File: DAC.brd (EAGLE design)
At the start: 81.3 x 82.5 mm, 101 parts, among them IC1 LM2662, IC2 PCM1793, IC3 OPA2134PA, IC4 LMH6643, J1 USBSMD, J2 RCJ-21XXMILL, U1 LDO-TPS78233, U2 PCM2707, Y1 12MHz/20pF

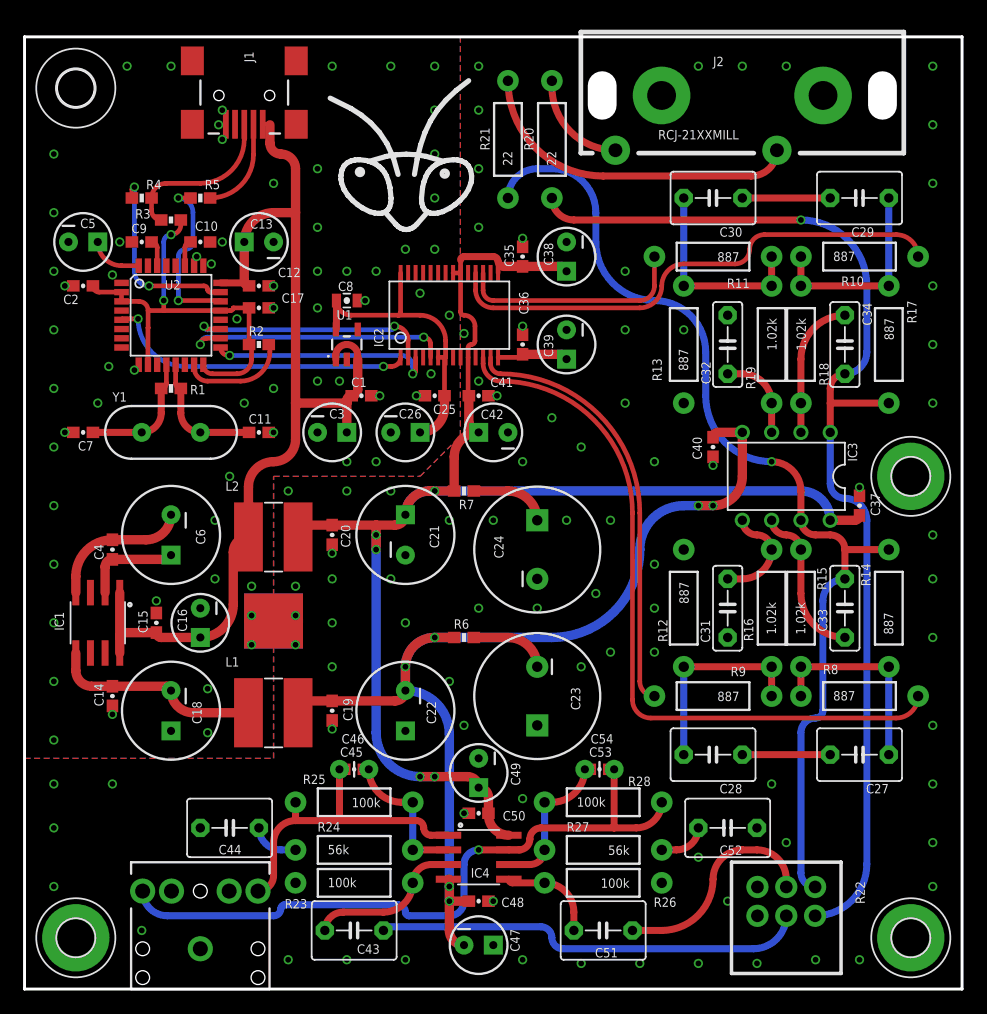
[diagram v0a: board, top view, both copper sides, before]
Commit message: PCB layout closer to guidelines
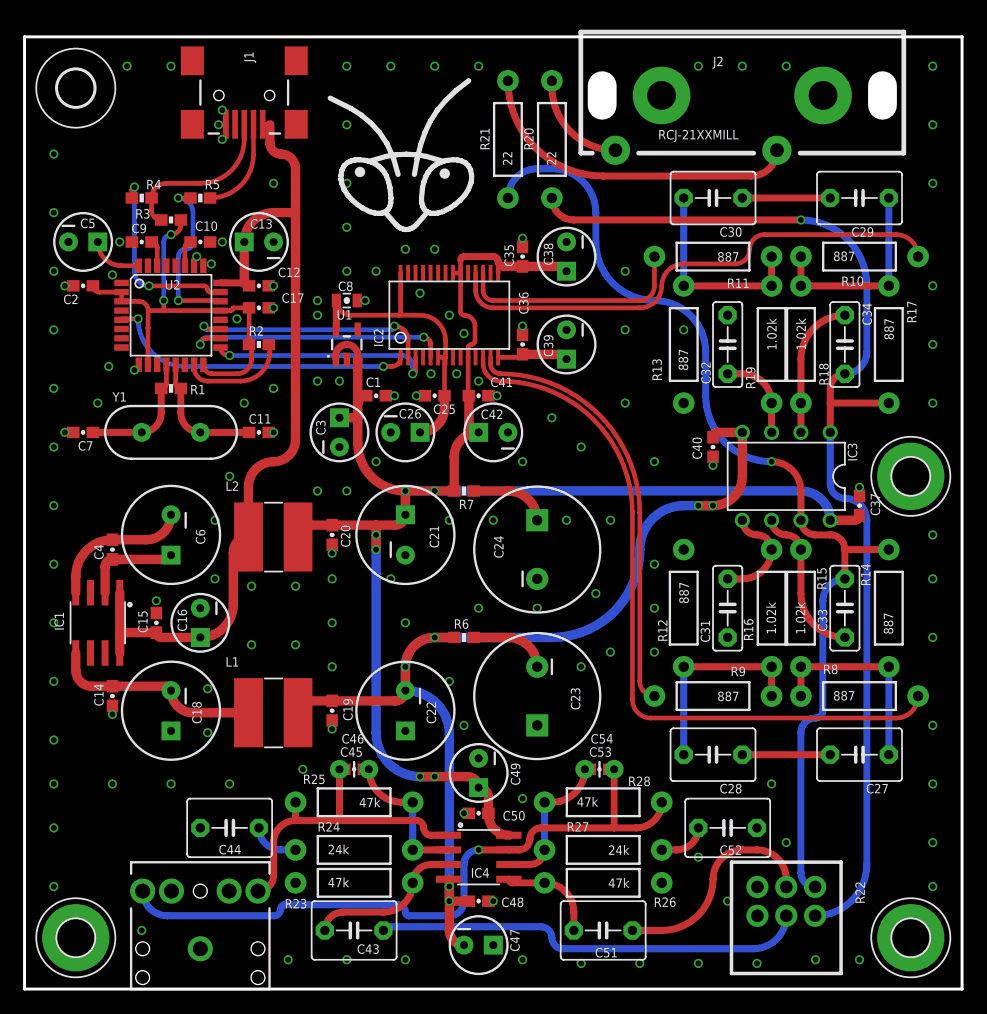
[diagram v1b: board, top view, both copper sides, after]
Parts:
- removed GB1, GB2: (no value), my:COPPER-BRIDGE
- R23, R25, R26, R28: value 100k -> 47k
- R24, R27: value 56k -> 24k
- moved C1 1.27 mm to (30.5, 51.4)
- moved C3 0.63 mm to (27.3, 48.3), turned to 90 degrees
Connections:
- removed net AGND: C19.1, C20.2, C21.2, C22.1, C23.+, C24.-, C31.1, C32.1, C35.2, C36.2, C37.2, C38.2, C39.2, C40.2, C41.2, C42.2, C44.1, C47.1, C48.2, C49.2, C50.2, C52.1, GB1.P$2.1, GB1.P$2.2, GB2.P$2.1, GB2.P$2.2, H1.B3,2, H2.B3,2, H3.B3,2, IC2.11, IC2.16, IC2.19, IC2.9, J2.1, J2.3, J3.SLEEVE, R12.P$1, R13.P$1, R22.R1.1, R22.R2.1, R23.P$1, R26.P$1
- net +5V: now also C1.1, C3.1, U1.1, U1.3
- net GND: now also C19.1, C20.2, C21.2, C22.1, C23.+, C24.-, C31.1, C32.1, C35.2, C36.2, C37.2, C38.2, C39.2, C40.2, C41.2, C42.2, C44.1, C47.1, C48.2, C49.2, C50.2, C52.1, H1.B3,2, H2.B3,2, H3.B3,2, IC2.11, IC2.16, IC2.19, IC2.9, J2.1, J2.3, J3.SLEEVE, R12.P$1, R13.P$1, R22.R1.1, R22.R2.1, R23.P$1, R26.P$1; no longer GB1.P$1.1, GB1.P$1.2, GB2.P$1.1, GB2.P$1.2
- net VCC: no longer C1.1, C3.1, U1.1, U1.3
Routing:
- net +5V: track 126.8 -> 148.3 mm, vias 5 -> 6
- net VCC: track 88.6 -> 74.1 mm
- removed copper zone on layer 1, net AGND
- removed copper zone on layer 16, net AGND

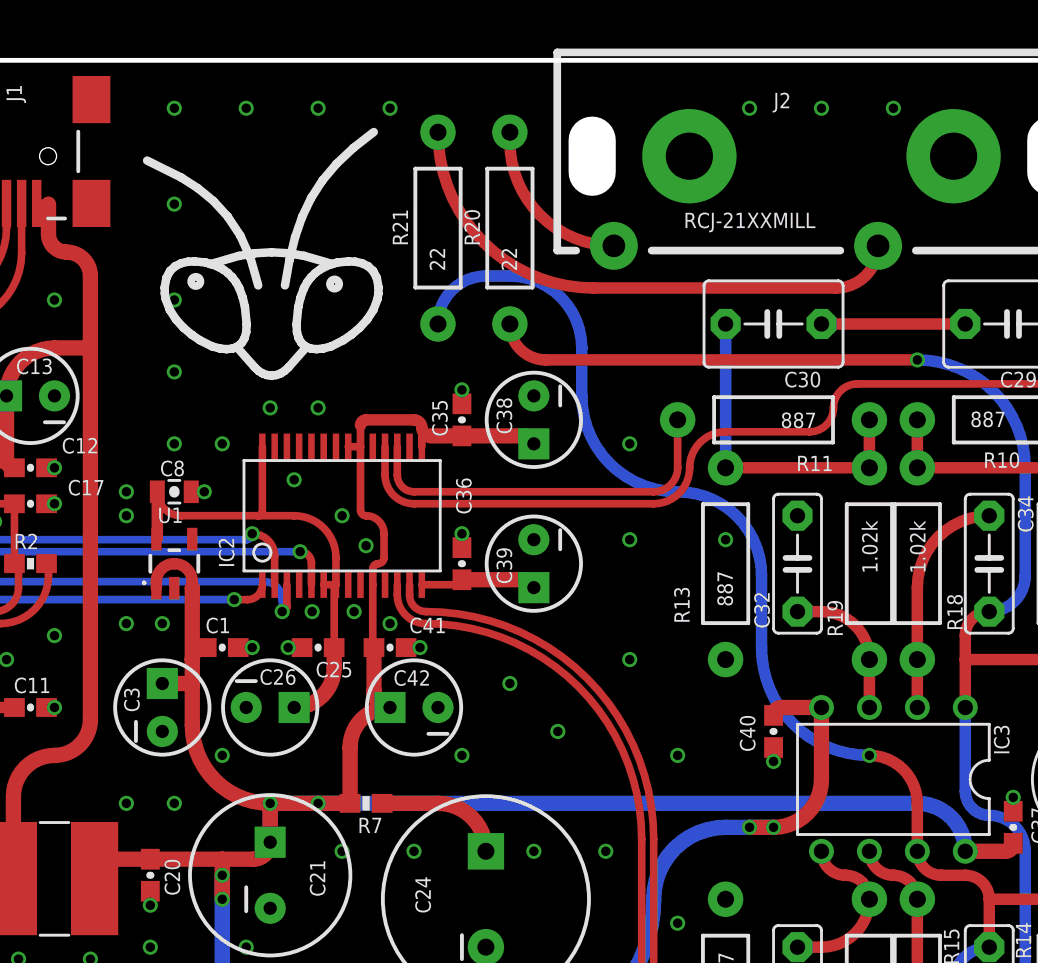
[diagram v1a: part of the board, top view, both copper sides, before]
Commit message: Power rerouted
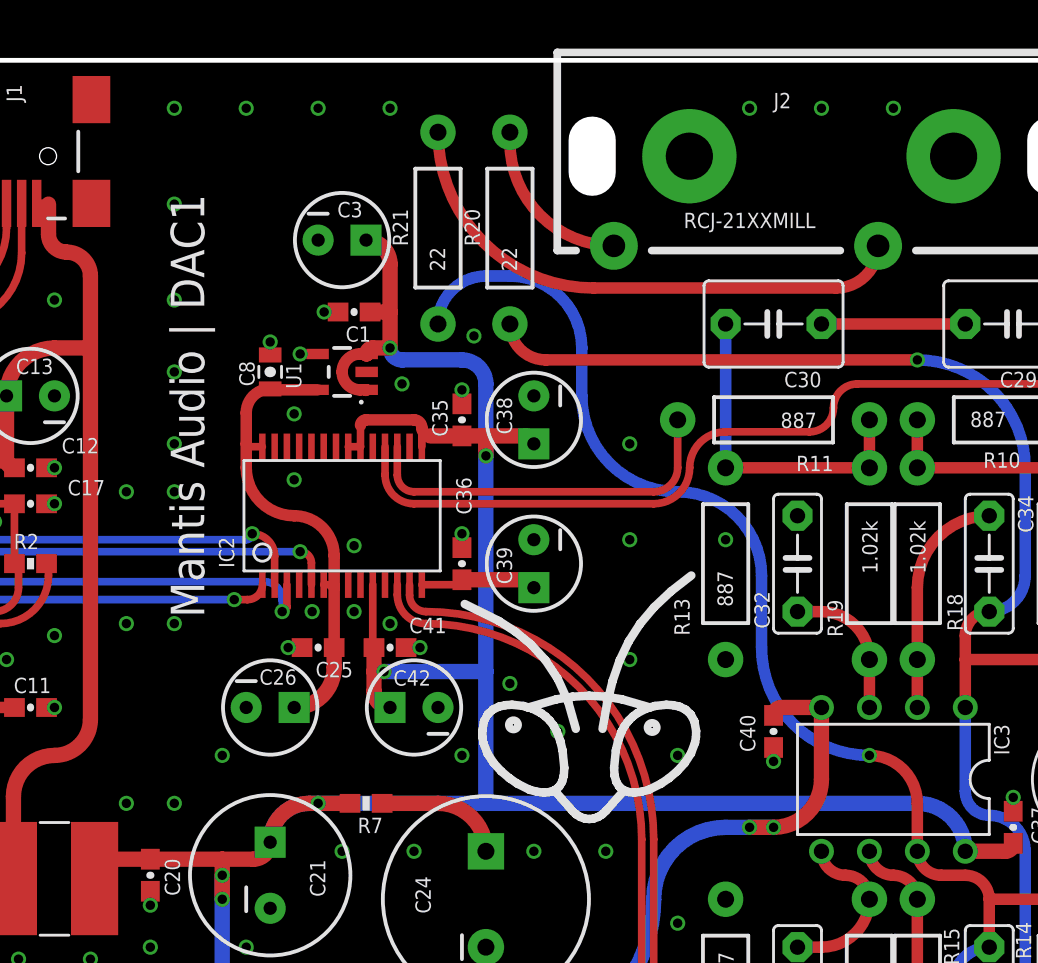
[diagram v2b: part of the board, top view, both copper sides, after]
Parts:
- moved LOGO1 28.9 mm to (49.8, 48.9)
- moved C3 26.5 mm to (36.8, 73.0), turned to 0 degrees
- moved C1 19.1 mm to (37.5, 69.2), turned to 180 degrees
- moved U1 13.5 mm to (36.8, 66.0), turned to 90 degrees
- moved C8 8.13 mm to (33.0, 66.0), turned to 90 degrees
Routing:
- net +5V: track 148.3 -> 159.9 mm, vias 6 -> 8
- net 3V3: track 26.7 -> 24.6 mm
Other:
- board text added: "Mantis Audio | DAC1"
